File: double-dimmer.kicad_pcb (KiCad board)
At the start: 2 copper layers, 84 x 56 mm, 12 parts, among them J1 Netzspannung, J2 Screw_Terminal_01x05, J3 Conn_01x04, SW1 SW_Push, SW2 SW_Push

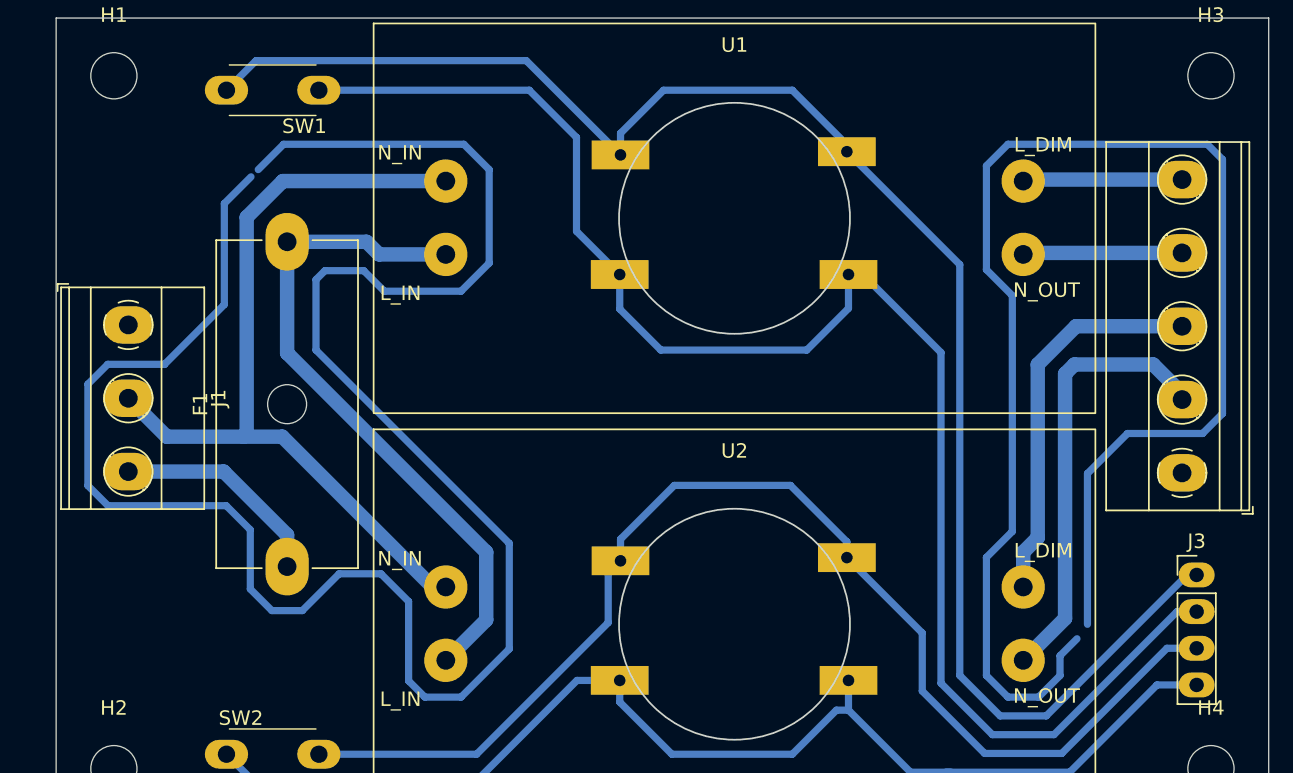
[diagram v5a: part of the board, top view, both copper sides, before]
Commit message: Add warning sign
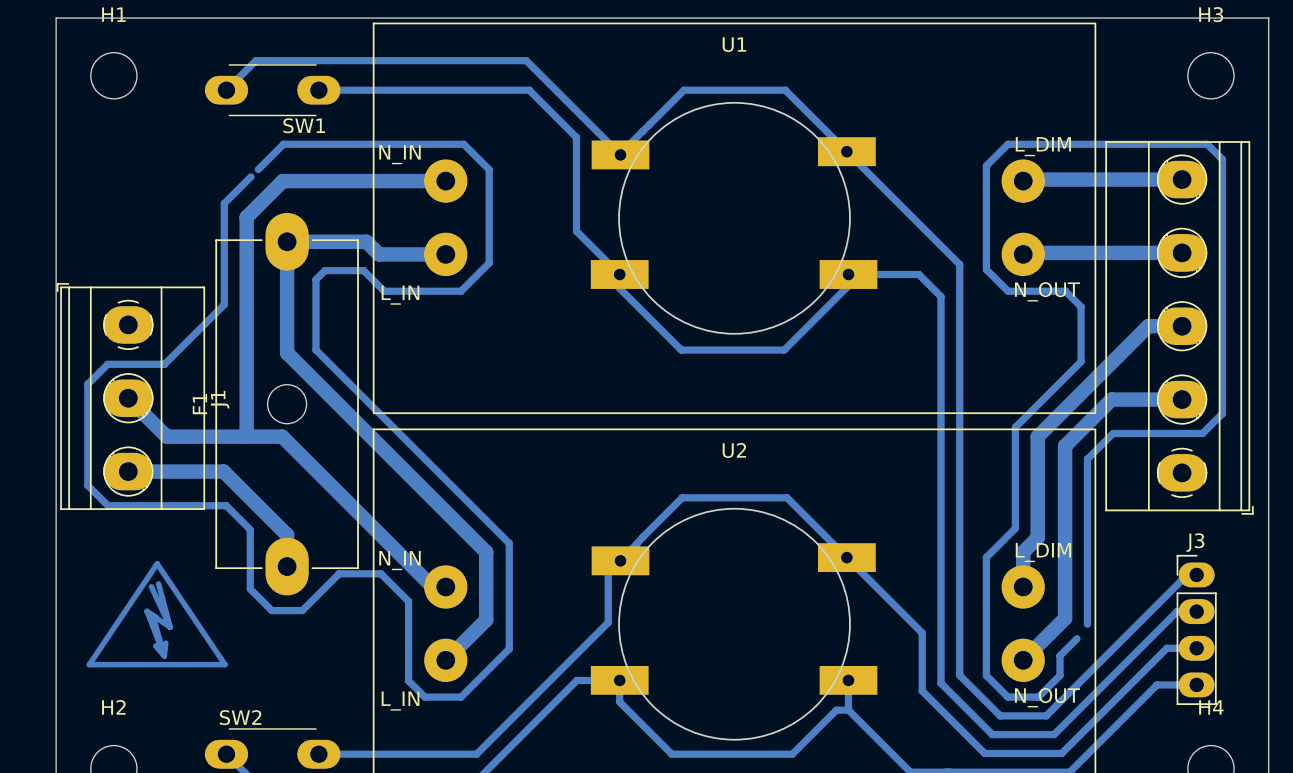
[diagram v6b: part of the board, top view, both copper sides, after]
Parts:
- added REF**: Symbol_HighVoltage_Type2_CopperTop_VerySmall, Symbol:Symbol_HighVoltage_Type2_CopperTop_VerySmall, B.Cu at (59.0, 97.0)
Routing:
- net (no net): track 244.2 -> 251.1 mm
- net N_OUT2: track 30.7 -> 25.5 mm
- net L_OUT2: track 26.9 -> 24.0 mm
- net Switch_A2: track 85.1 -> 82.9 mm
- net Switch_A1: track 112.5 -> 111.3 mm
- net Switch_B1: track 107.2 -> 107.7 mm

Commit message: Add drill place origin
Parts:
- moved F1 49.2 mm to (116.0, 82.0)
- moved H1 49.2 mm to (104.0, 48.0)
- moved H2 49.2 mm to (104.0, 96.0)
- moved H3 49.2 mm to (180.0, 48.0)
- moved H4 49.2 mm to (180.0, 96.0)
- moved J1 49.2 mm to (105.0, 65.3)
- moved J2 49.2 mm to (178.0, 75.5)
- moved J3 49.2 mm to (179.0, 82.6)
- moved REF** 49.2 mm to (107.0, 86.0)
- moved SW1 49.2 mm to (118.2, 49.0)
- moved SW2 49.2 mm to (111.8, 95.0)
- moved U1 49.2 mm to (147.0, 57.9)
- moved U2 49.2 mm to (147.0, 86.0)

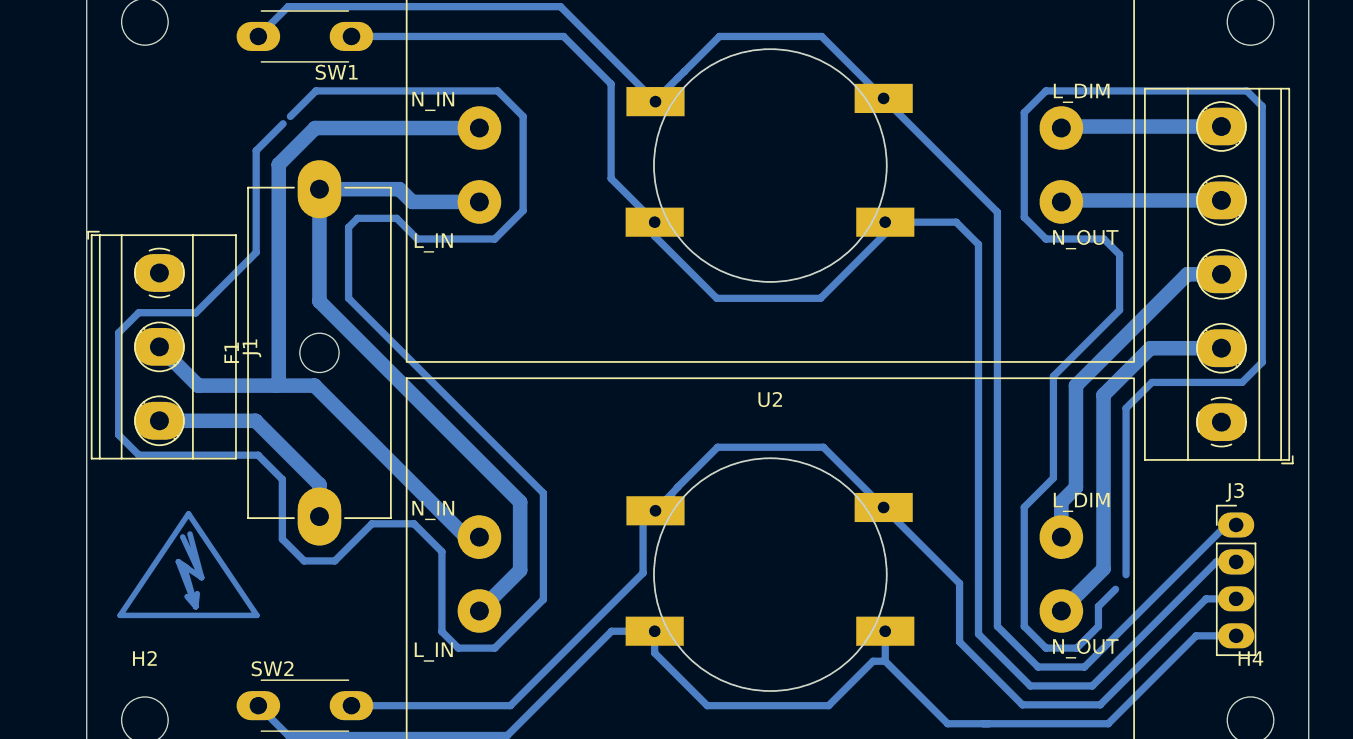
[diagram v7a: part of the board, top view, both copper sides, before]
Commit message: Plotting the PCB + step file
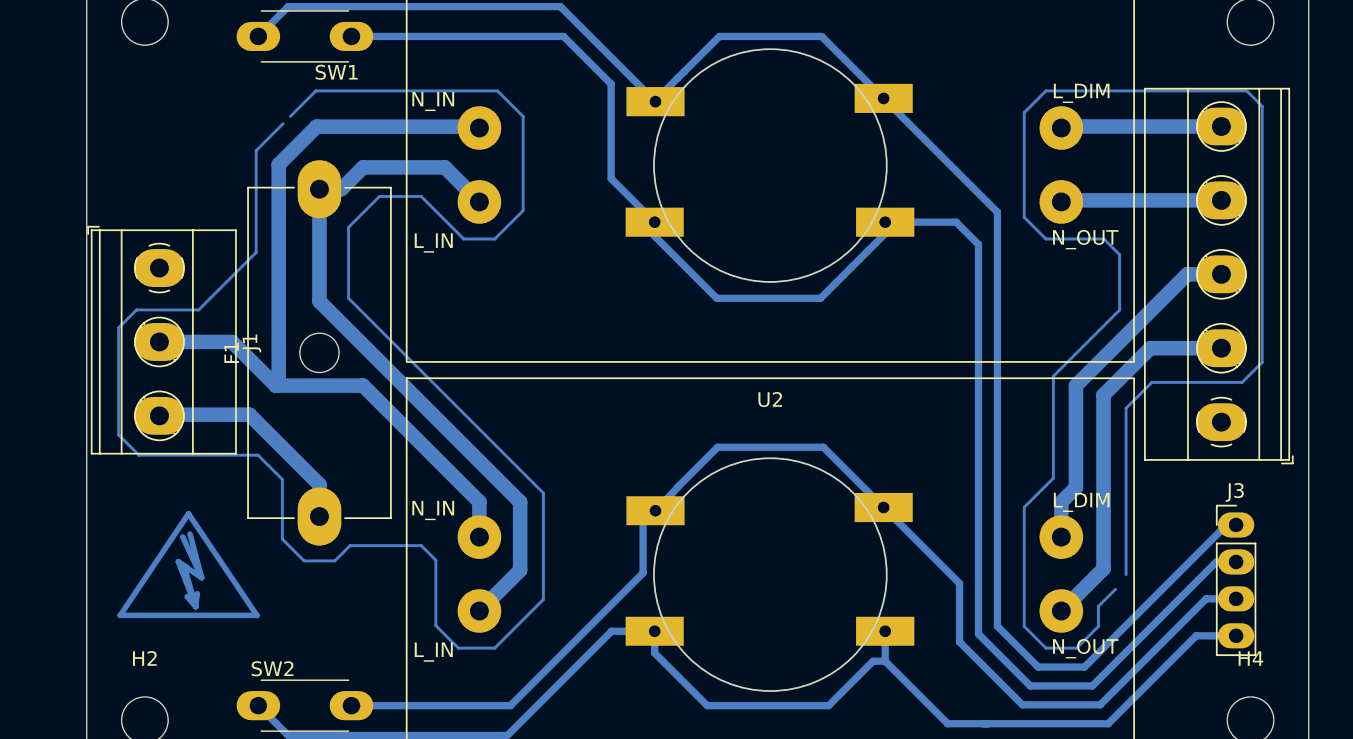
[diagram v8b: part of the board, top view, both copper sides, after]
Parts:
- moved J1 0.34 mm to (105.0, 64.9)
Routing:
- net N: track 57.5 -> 59.2 mm
- net L: track 47.2 -> 48.5 mm
